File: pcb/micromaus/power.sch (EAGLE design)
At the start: 27 parts, among them IC1 AD712R, Q1 BSL307SP, T1 BC847, T2 BC847, U1 LP3965EMP-3.3

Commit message: improved power supply
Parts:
- added C10, C9: 1n, rcl:C-EUC0603
- added R13: 33k, rcl:R-EU_R0603
- C2: value (none) -> 33u
- R1, R2: value (none) -> 22k
- R11: value 22k -> 100k
- R12: value 400k -> 100k
- R4: value 100k -> 470k
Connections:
- removed net BOOST_EN: R4.2, U$1.EN
- removed net N$12: R10.1, T2.B
- removed net N$13: R11.2, T1.B
- removed net VBUS_EN: IC1A.OUT, Q1.G, R12.2, R4.1
- new net /VBUS_EN: IC1A.OUT, Q1.G, R9.2
- new net BUCK_EN: C10.1, R11.2, R4.1, U$1.EN
- new net N$1: R9.1, T1.C, T2.B
- new net VSENSE: C9.1, R12.1, R13.2
- net +5V: now also R10.2; no longer T1.C, T2.C
- net EN_3V3: now also R10.1, T2.C; no longer R9.2, T1.E, T2.E
- net GND: now also C10.2, C9.2, R11.1, R13.1, T1.E, T2.E; no longer R9.1
- net PGOOD: now also T1.B; no longer R10.2
- net USB_VBUS: no longer R11.1
- net VBAT: now also R12.2, R4.2; no longer R12.1
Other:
- note added: "Sollte bei nichtanschluss einer Batterie 5V auf VBAT liegen, sorgt dieser Spannungsteiler dafür, dass an BOOST_EN eine Spannung von nur 1.02V anliegt. Das ist laut Datenblatt unter der Schwelle von 1.16V um den converter zu aktivieren. VBUS_EN wird bei 6.6V aktiv. Dann liegt hier schon 1.3V an, und das liegt über der Schwelle. Damit wird dann der converter aktiv. bei 15V und 470kOhm fließen auch 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"
- note added: "deiese krummen werte aus dem datenblatt scheinen mit sehr viel sorgfalt gewählt, damit kommt man auf 5.001 volt oder so"
- note added: "es soll die 3v3-Leitung an gehen, wenn das Gerät über USB (VBUS_EN) betrieben wird oder der Buck stabil ist (PGOOD) PGOOD or VBUS_EN => EN_3V3 de morgan <=> not (not PGOOD and not VBUS_EN) => EN_3V3 (not VBUS_EN) haben wir als signal, das wird mit dem ersten Transistor mit PGOOD vernandet. der zweite Transistor invertiert nur. wenn ich hier nur open drain mit pullups verwende, brauche ich keine v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"
- note added: "paranoia cap"
- note added: "somit ist die maximal moeglich messbare eingangsspannung 13.3 Volt. (3.3V am ESP32) das macht bei 11 bit knapp 6.5mV auflösung"
- note added: "todo hier einen p-kanal mosfet aussuchen muss das ein depletion type sein?"
- note removed: "Die widerstandswerte hier sind noch zu durchdenken, es gibt einen maximalstrom für BOOST_EN. idee ist: beim hochfahren von Batterie ist VBUS_EN erst mal undefiniert und wird nicht getrieben (hoffentlich) weil der komparator keinen Strom bekommt. dann zieht VBAT das hoch."
- note removed: "alternativ EN des MP2333H an den ausgang des opamp? muss dann der AD712R an VBAT betrieben werden?"
- note removed: "alternativ dioden-or?"
- note removed: "muss das ein depletion type sein?"
- note removed: "todo widerstandswerte"
- moved on the sheet: C3, C4, C5, C6, C7, C8, L1, R10, R11, R12, R3, R4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

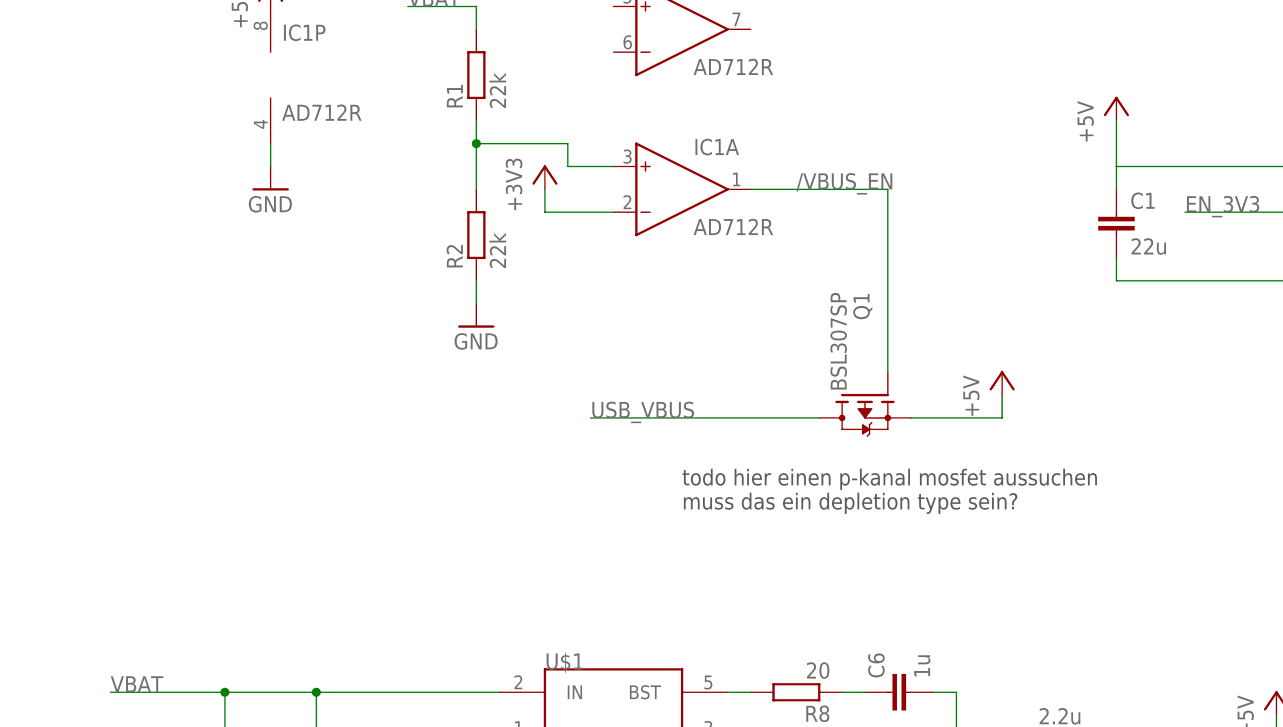
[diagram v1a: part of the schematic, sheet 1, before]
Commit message: added xt60 input to power supply
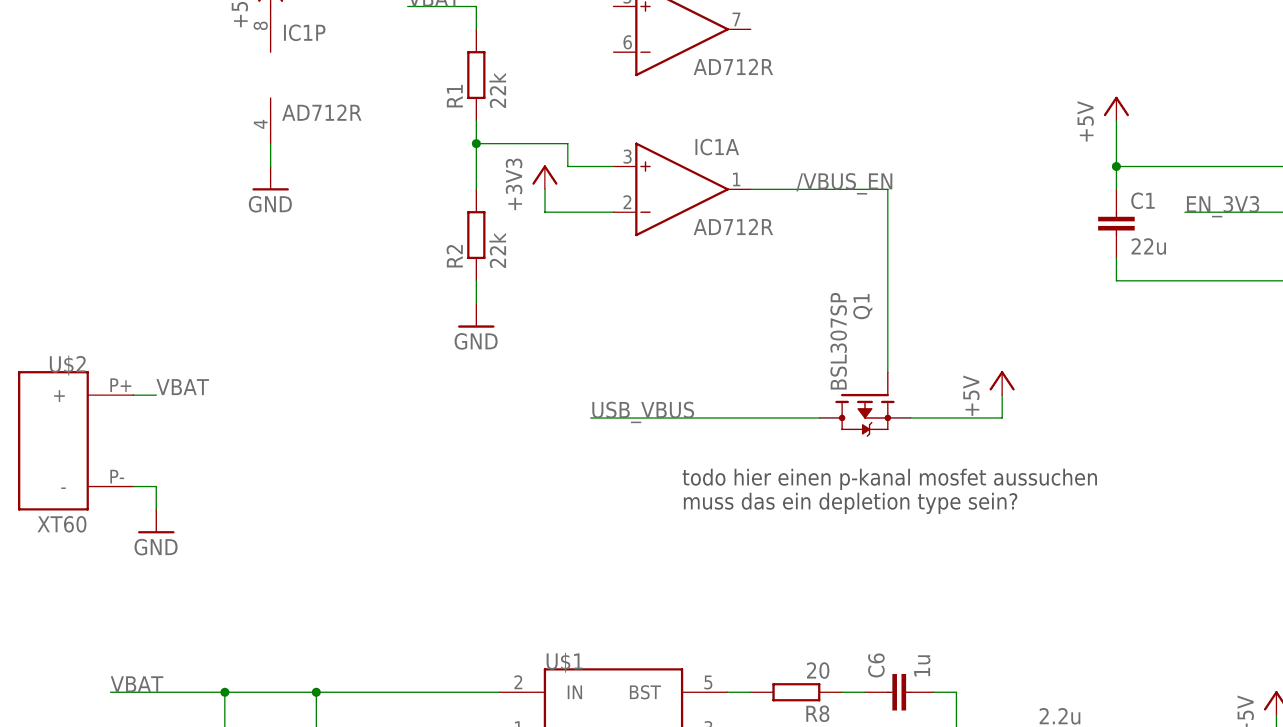
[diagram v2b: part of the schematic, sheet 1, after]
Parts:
- added U$2: XT60, xt60:XT60
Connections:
- net GND: now also U$2.-
- net VBAT: now also U$2.+
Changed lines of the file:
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@@
 <part name="C9" library="rcl" library_urn="urn:adsk.eagle:library:334" deviceset="C-EU" device="C0603" package3d_urn="urn:adsk.eagle:package:23616/2" value="1n"/>
 <part name="C10" library="rcl" library_urn="urn:adsk.eagle:library:334" deviceset="C-EU" device="C0603" package3d_urn="urn:adsk.eagle:package:23616/2" value="1n"/>
+<part name="U$2" library="xt60" deviceset="XT60" device=""/>
+<part name="GND15" library="supply1" library_urn="urn:adsk.eagle:library:371" deviceset="GND" device=""/>
 </parts>
 <sheets>
@@
 <attribute name="VALUE" x="52.324" y="-52.959" size="1.778" layer="96"/>
 </instance>
+<instance part="U$2" gate="G$1" x="-121.92" y="20.32" smashed="yes" rot="MR0">
+<attribute name="NAME" x="-119.38" y="27.94" size="1.778" layer="95" rot="MR0"/>
+<attribute name="VALUE" x="-119.38" y="10.16" size="1.778" layer="96" rot="MR0"/>
+</instance>
+<instance part="GND15" gate="1" x="-111.76" y="10.16" smashed="yes">
+<attribute name="VALUE" x="-114.3" y="7.62" size="1.778" layer="96"/>
+</instance>
 </instances>
 <busses>
@@
 <wire x1="111.76" y1="40.64" x2="111.76" y2="43.18" width="0.1524" layer="91"/>
 </segment>
+<segment>
+<pinref part="U$2" gate="G$1" pin="-"/>
+<pinref part="GND15" gate="1" pin="GND"/>
+<wire x1="-114.3" y1="15.24" x2="-111.76" y2="15.24" width="0.1524" layer="91"/>
+<wire x1="-111.76" y1="15.24" x2="-111.76" y2="12.7" width="0.1524" layer="91"/>
+</segment>
 </net>
 <net name="+5V" class="0">
@@
 <wire x1="-5.08" y1="55.88" x2="-5.08" y2="50.8" width="0.1524" layer="91"/>
 <wire x1="-5.08" y1="50.8" x2="20.32" y2="50.8" width="0.1524" layer="91"/>
+<junction x="-5.08" y="50.8"/>
 </segment>
 <segment>
@@
 <label x="99.06" y="71.12" size="1.778" layer="95"/>
 </segment>
+<segment>
+<pinref part="U$2" gate="G$1" pin="+"/>
+<wire x1="-114.3" y1="25.4" x2="-111.76" y2="25.4" width="0.1524" layer="91"/>
+<label x="-111.76" y="25.4" size="1.778" layer="95"/>
+</segment>
 </net>
 <net name="N$5" class="0">
@@
 </sheet>
 </sheets>
+<errors>
+</errors>
 </schematic>
 </drawing>
